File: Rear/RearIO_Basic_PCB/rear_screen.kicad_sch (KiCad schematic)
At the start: 48 parts, among them J1 Conn_01x02_Pin, J13 USB_C_Receptacle_USB2.0, J2 Conn_01x02_Pin, J3 Conn_01x02_Pin, J4 Conn_01x02_Pin, J5 Conn_01x02_Pin, J6 Conn_01x02_Pin, J7 Conn_01x08_Socket, Q1 NTMFS4C03N-HXY, Q2 NTMFS4C03N-HXY, Q3 NTMFS4C03N-HXY, Q4 NTMFS4C03N-HXY, Q6 NTMFS4C03N-HXY, Q7 NTMFS4C03N-HXY, U1 MIC4426, U2 MIC4426, U3 AOZ1280CI

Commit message: wip
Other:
- note added: "Port HP1"
- note added: "Port HP2"
- note added: "Port LP1"
- note added: "Port LP2"
- note added: "Screen Connector (1.25mmx8P)"
- note removed: "Screen COnnector (1.25mmx8P)"
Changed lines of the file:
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@@
+    (effects (font (size 1.27 1.27)) (justify left bottom))
+  )
+  (text "Port HP2" (at 116.586 74.422 0)
     (effects (font (size 1.27 1.27)) (justify left bottom))
   )
@@
     (effects (font (size 1.27 1.27)) (justify left bottom))
   )
-  (text "Screen COnnector (1.25mmx8P)" (at 233.426 37.338 0)
+  (text "Screen Connector (1.25mmx8P)" (at 233.426 37.338 0)
     (effects (font (size 1.27 1.27)) (justify left bottom))
   )
@@
     (effects (font (size 1.27 1.27)) (justify left bottom))
   )
+  (text "Port HP1" (at 116.586 43.434 0)
+    (effects (font (size 1.27 1.27)) (justify left bottom))
+  )
+  (text "Port LP2" (at 116.84 136.398 0)
+    (effects (font (size 1.27 1.27)) (justify left bottom))
+  )
+  (text "Port LP1" (at 116.84 106.172 0)
+    (effects (font (size 1.27 1.27)) (justify left bottom))
+  )

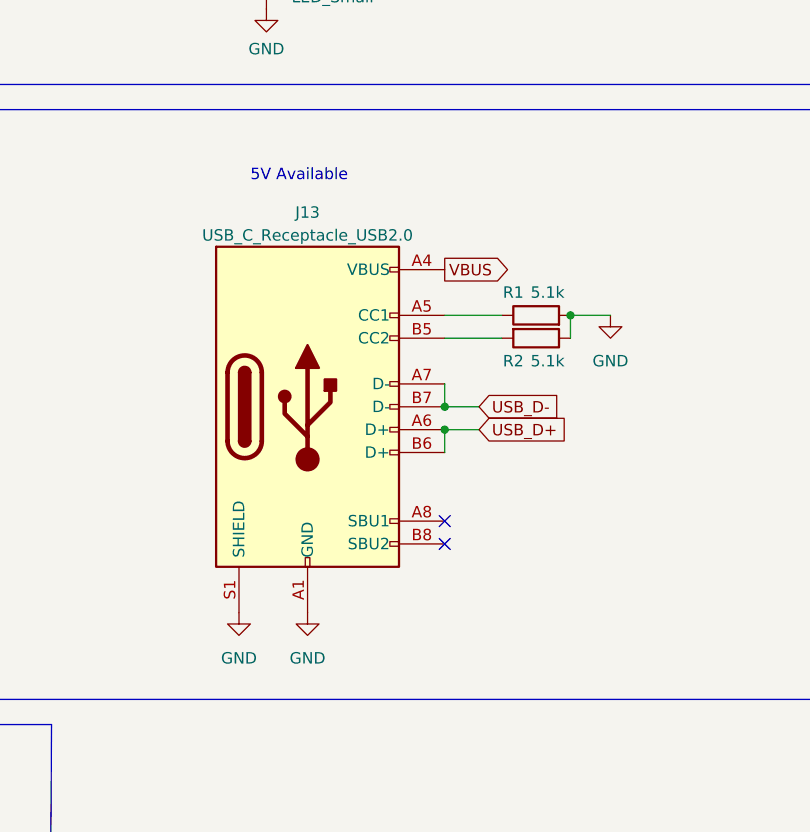
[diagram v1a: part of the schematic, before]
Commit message: small routing and layout changes, removed USB
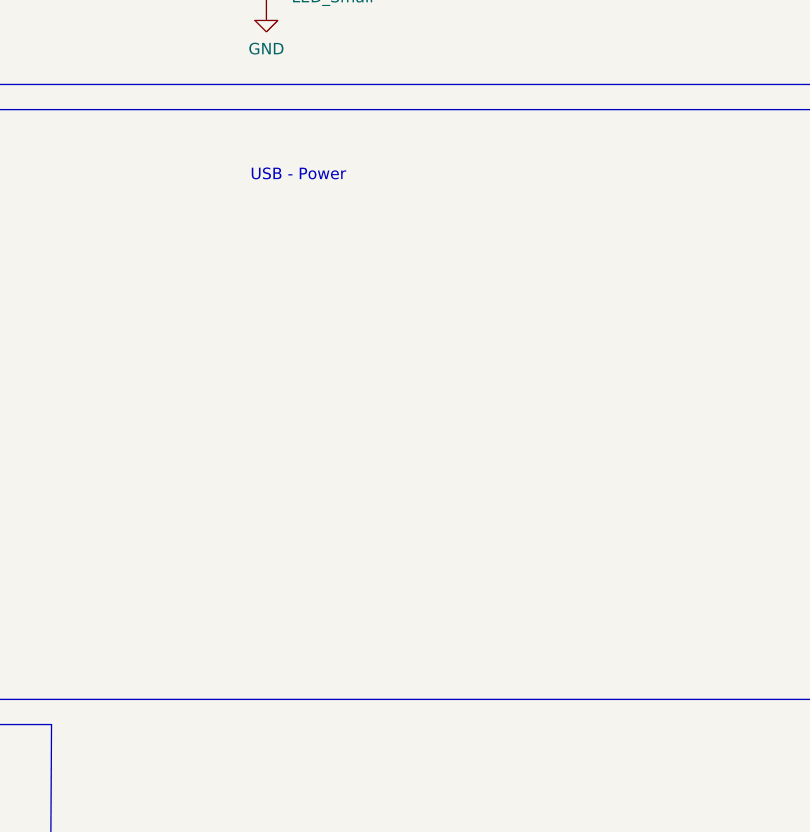
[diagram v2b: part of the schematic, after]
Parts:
- removed J13: USB_C_Receptacle_USB2.0, Connector_USB:USB_C_Receptacle_G-Switch_GT-USB-7010ASV, symbol Connector:USB_C_Receptacle_USB2.0
- removed R1, R2: 5.1k, Resistor_SMD:R_0603_1608Metric, symbol Device:R
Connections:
- no-connect marks 4 -> 2
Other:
- note added: "USB - Power"

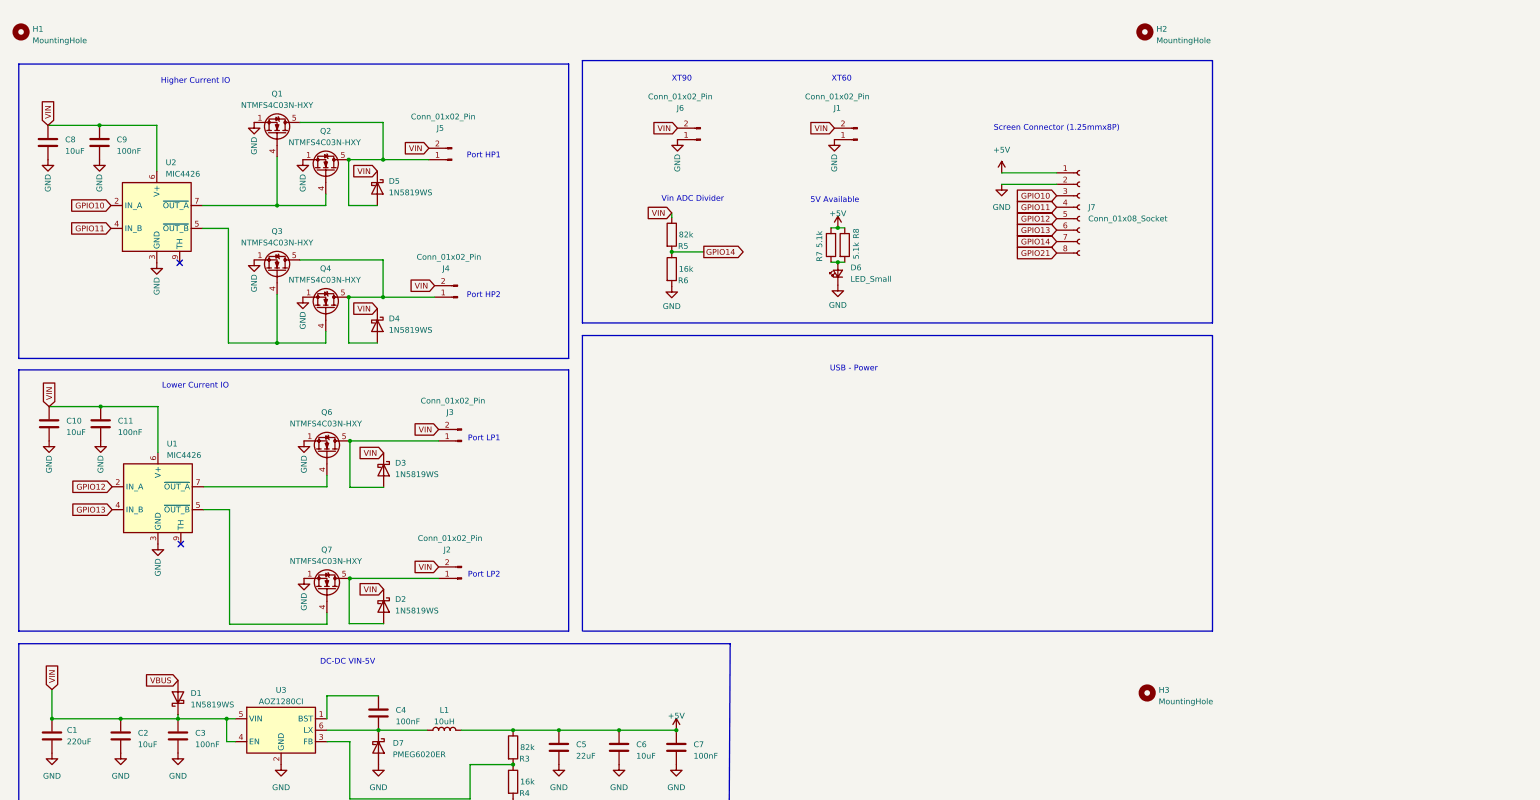
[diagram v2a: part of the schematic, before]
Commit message: routing and layout changes
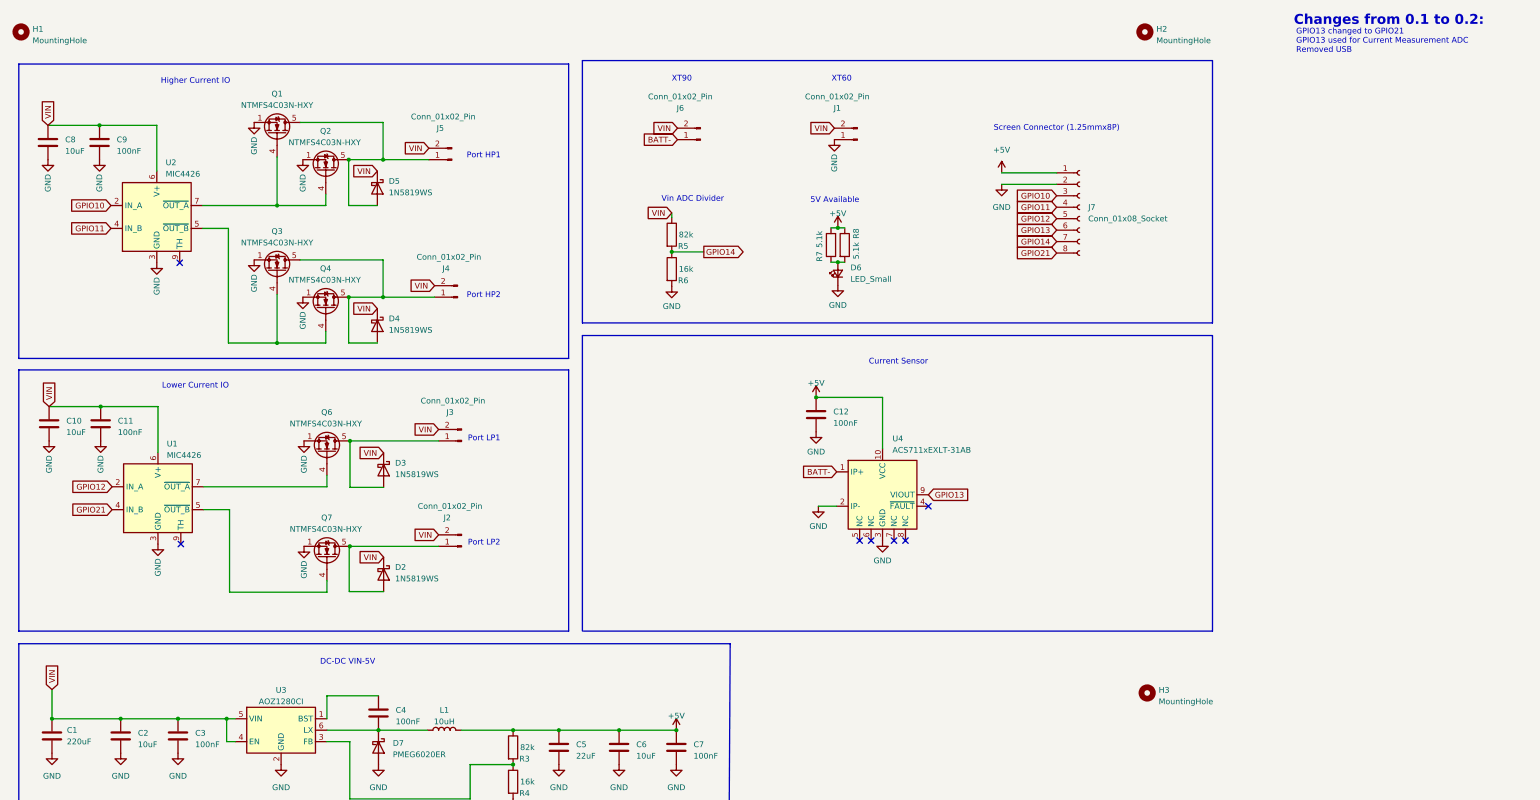
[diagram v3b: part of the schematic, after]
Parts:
- removed D1: 1N5819WS, Diode_SMD:D_SOD-323, symbol Diode:1N5819WS
- added C12: 100nF, Capacitor_SMD:C_0603_1608Metric, symbol Device:C
- added U4: ACS711xEXLT-31AB, Sensor_Current:Allegro_QFN-12-10-1EP_3x3mm_P0.5mm, symbol Sensor_Current:ACS711xEXLT-31AB
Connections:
- net +5V: now also C12.1, U4.10 (VCC)
- net GND: now also C12.2, U4.2 (IP-), U4.3 (GND); no longer J6.1 (Pin_1)
- net GPIO13: now also U4.9 (VIOUT); no longer U1.4 (IN_B)
- net GPIO21: now also U1.4 (IN_B)
- new net BATT-: J6.1 (Pin_1), U4.1 (IP+)
- no-connect marks 2 -> 7
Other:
- note added: "Changes from 0.1 to 0.2:"
- note added: "Current Sensor"
- note added: "GPIO13 changed to GPIO21 GPIO13 used for Current Measurement ADC Removed USB"
- note removed: "USB - Power"
- moved on the sheet: D2, J2, Q7
